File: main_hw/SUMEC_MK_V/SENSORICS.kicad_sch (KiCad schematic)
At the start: 18 parts, among them J10 Conn_01x03_Pin, J11 Conn_01x03_Pin, J12 Conn_01x03_Pin, J13 Conn_01x03_Pin, J14 Conn_01x03_Pin, J15 Conn_01x03_Pin, J5 Conn_01x04_Pin, J6 Conn_01x06_Pin, J7 Conn_01x06_Pin, J8 Conn_01x03_Pin, J9 Conn_01x06_Pin, U7 BMI088

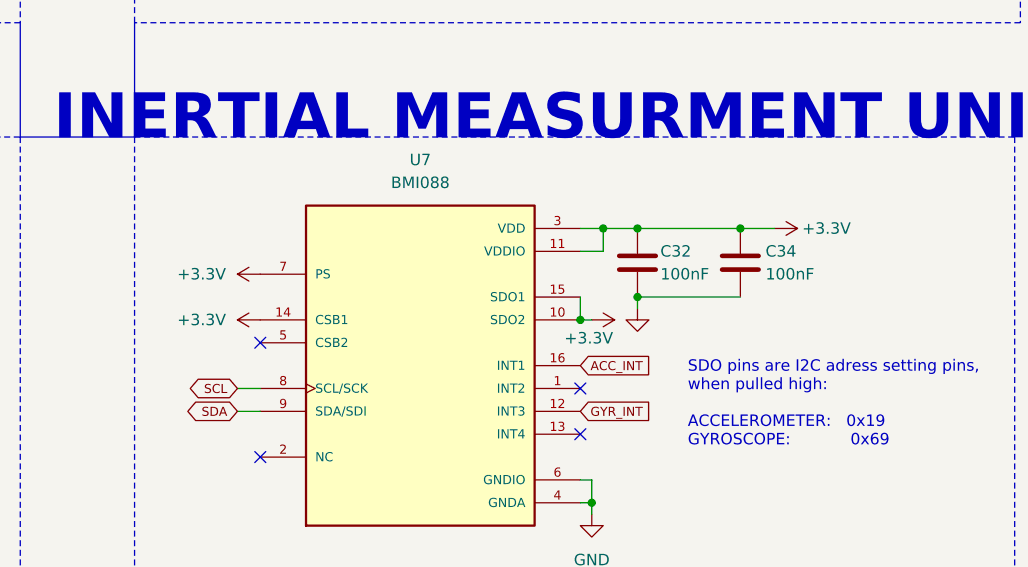
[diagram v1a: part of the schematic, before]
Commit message: PCB Update, signal routing
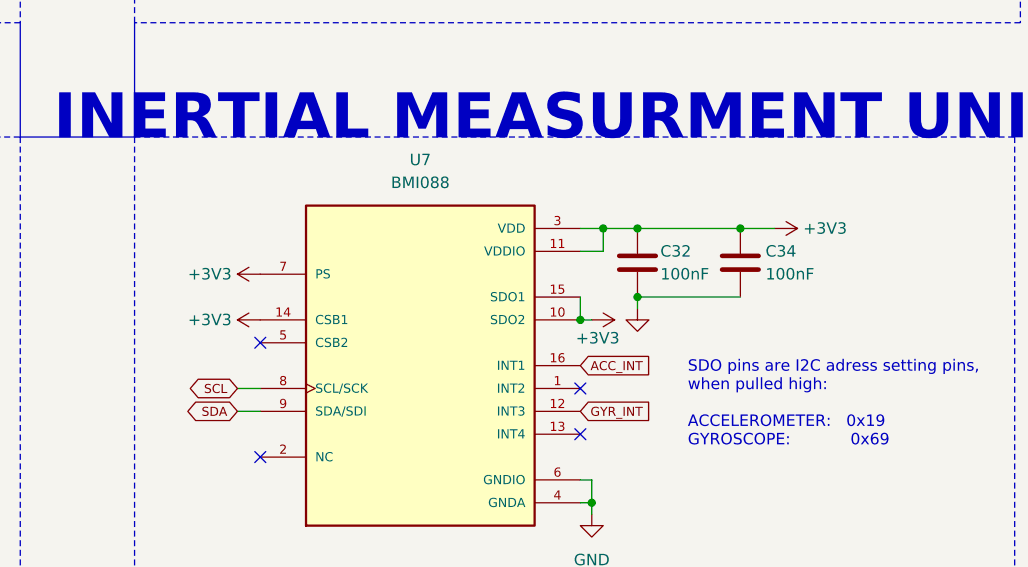
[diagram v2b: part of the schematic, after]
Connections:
- net +3.3V is gone; now on net +3V3: C32.2, C34.2, U7.10 (SDO2), U7.11 (VDDIO), U7.14 (CSB1), U7.15 (SDO1), U7.3 (VDD), U7.7 (PS)

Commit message: a lot of routing and layout updates
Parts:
- removed J7, J9: Conn_01x06_Pin, Connector_Molex:Molex_PicoBlade_53398-0671_1x06-1MP_P1.25mm_Vertical, symbol Connector:Conn_01x06_Pin
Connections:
- no-connect marks 7 -> 5
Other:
- moved on the sheet: J6

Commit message: sumec pcb update
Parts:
- renumbered C31 to C28, C32 to C29, C33 to C30, C34 to C31, J12 to J10, J13 to J11, J14 to J12, J15 to J13, J8 to J7, J10 to J8, J11 to J9, R34 to R28, R35 to R29, U7 to U6
